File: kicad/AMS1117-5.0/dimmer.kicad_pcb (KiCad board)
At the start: 2 copper layers, 25.4 x 35.6 mm, 12 parts, among them IC1 ATTINY85-S, P1 CONN_01X02, P2 CONN_01X02, Q1 Q_NMOS_GDS, SW2 TACTILE_SW, SW4 TACTILE_SW, U1 MC78L05ACH

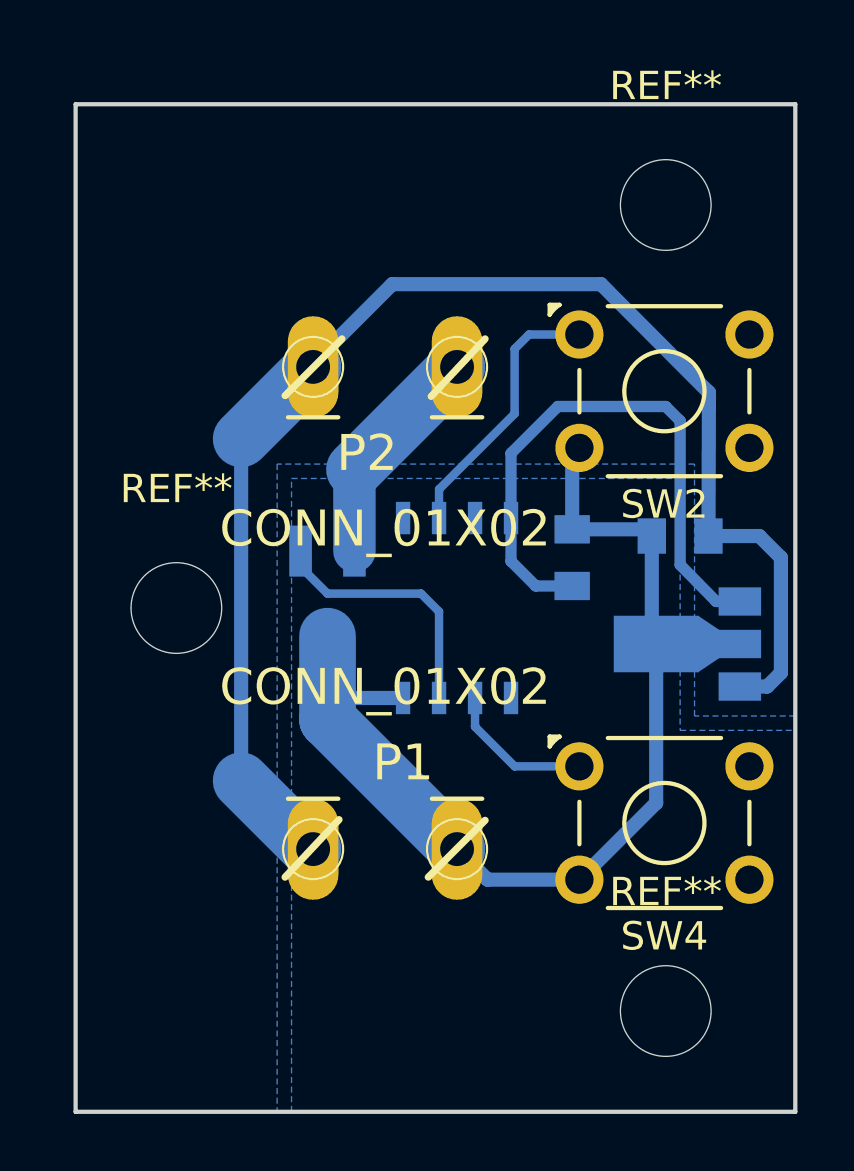
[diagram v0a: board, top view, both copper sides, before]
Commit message: AMS1117-5.0 regulator version
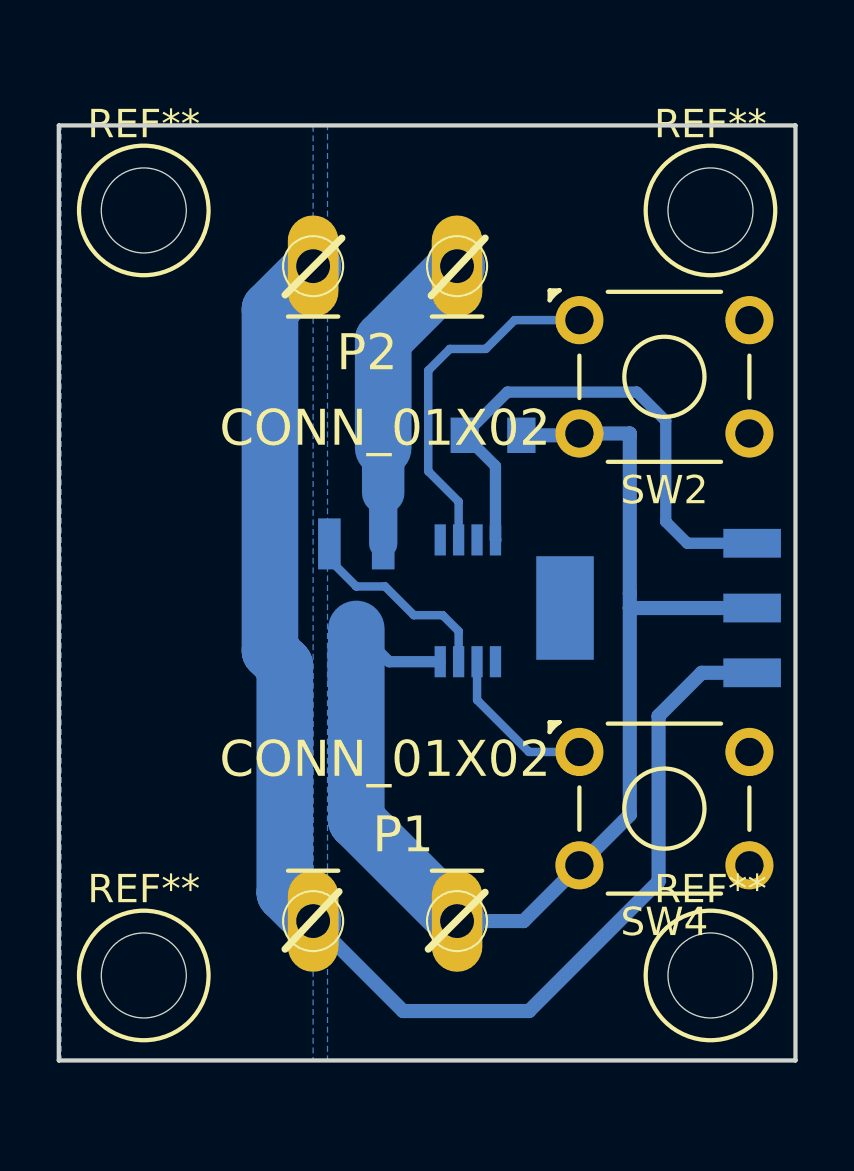
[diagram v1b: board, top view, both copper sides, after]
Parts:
- removed the REF** at (201.4, 143.3)
- removed the REF** at (201.4, 114.8)
- removed the REF** at (184.2, 129.0)
- added REF**: 1pin, Connect:1pin, F.Cu at (183.0, 115.0)
- added REF**: 1pin, Connect:1pin, F.Cu at (183.0, 142.0)
- added REF**: 1pin, Connect:1pin, F.Cu at (203.0, 142.0)
- added REF**: 1pin, Connect:1pin, F.Cu at (203.0, 115.0)
- IC1: value ATTINY85-S -> ATTINY85-P; footprint SMD_Packages:SOIC-8-N -> Housings_SSOP:TSSOP-8_3x3mm_Pitch0.65mm
- U1: footprint TO_SOT_Packages_SMD:SOT89-3_Housing -> TO_SOT_Packages_SMD:SOT-223
- moved C1 13.7 mm to (189.0, 131.1), turned to 0 degrees
- moved C2 5.14 mm to (195.3, 122.9), turned to 0 degrees
- moved P2 3.56 mm to (191.5, 116.3)
- moved P1 2.54 mm to (191.5, 140.7)
- moved U1 1.63 mm to (201.2, 129.0)
- moved Q1 1.05 mm to (190.5, 128.3)
- moved SW4 0.51 mm to (198.4, 134.1)
- moved SW2 0.51 mm to (198.4, 118.9)
- moved IC1 0.46 mm to (194.4, 128.8), turned to 90 degrees
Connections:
- IC1 pad 1: (no net) -> Net-(IC1-Pad1)
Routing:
- net GND: track 39.8 -> 46.1 mm
- net Net-(IC1-Pad6): track 9.57 -> 12.7 mm
- net /out: track 8.00 -> 10.9 mm
- net Net-(IC1-Pad3): track 9.14 -> 7.24 mm
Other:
- board size 25.4 x 35.6 mm -> 26 x 33 mm
- net class 5V: via_dia 0.6 -> 1.5; via_drill 0.4 -> 0.8

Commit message: AMS1117 correct footprint
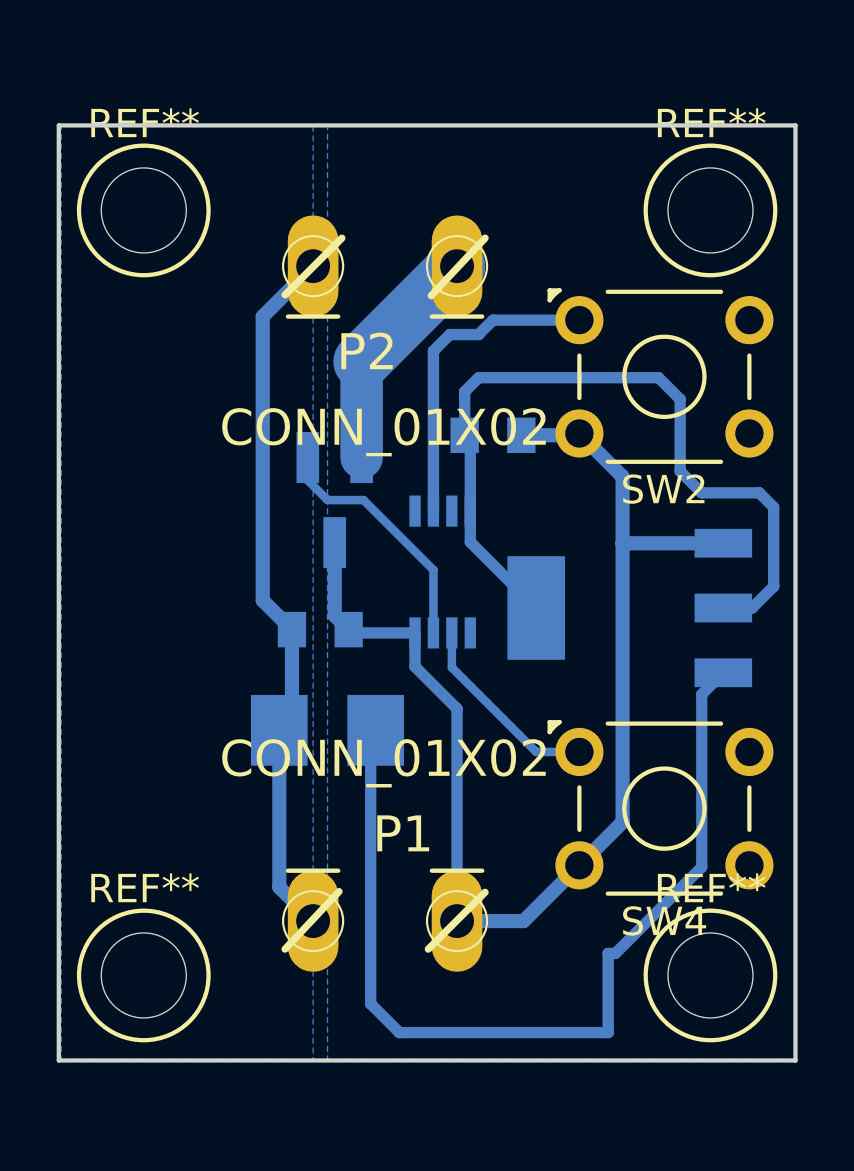
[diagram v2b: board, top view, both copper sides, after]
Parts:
- added D1: D_Small, Diodes_SMD:DO-214BA, B.Cu at (189.5, 133.3)
- IC1: value ATTINY85-P -> ATTINY85-S
- U1: value MC78L05ACH -> AMS1117-5.0
- moved Q1 3.14 mm to (189.7, 125.2)
- moved IC1 1.35 mm to (193.5, 127.8)
- moved C1 1.30 mm to (189.2, 129.8)
- moved U1 1.02 mm to (200.2, 129.0)
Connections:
- IC1 pad 1: Net-(IC1-Pad1) -> (no net)
- U1 pad 1: +5V -> GND
- U1 pad 2: GND -> +5V
- U1 pad 3: +12V -> Net-(D1-Pad1)
- U1 pad 4: (no net) -> +5V
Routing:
- net Net-(D1-Pad1): track 0.00 -> 33.1 mm
- net +12V: track 49.6 -> 25.0 mm
- net +5V: track 21.2 -> 28.1 mm
- net /out: track 10.9 -> 8.15 mm
- net Net-(IC1-Pad3): track 7.24 -> 8.82 mm
- net Net-(IC1-Pad6): track 12.7 -> 11.3 mm
- net Net-(IC1-Pad2): track 5.72 -> 6.96 mm
- net GND: track 46.1 -> 45.4 mm

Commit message: AMS117 PCB version: fixed attyny85 footprint
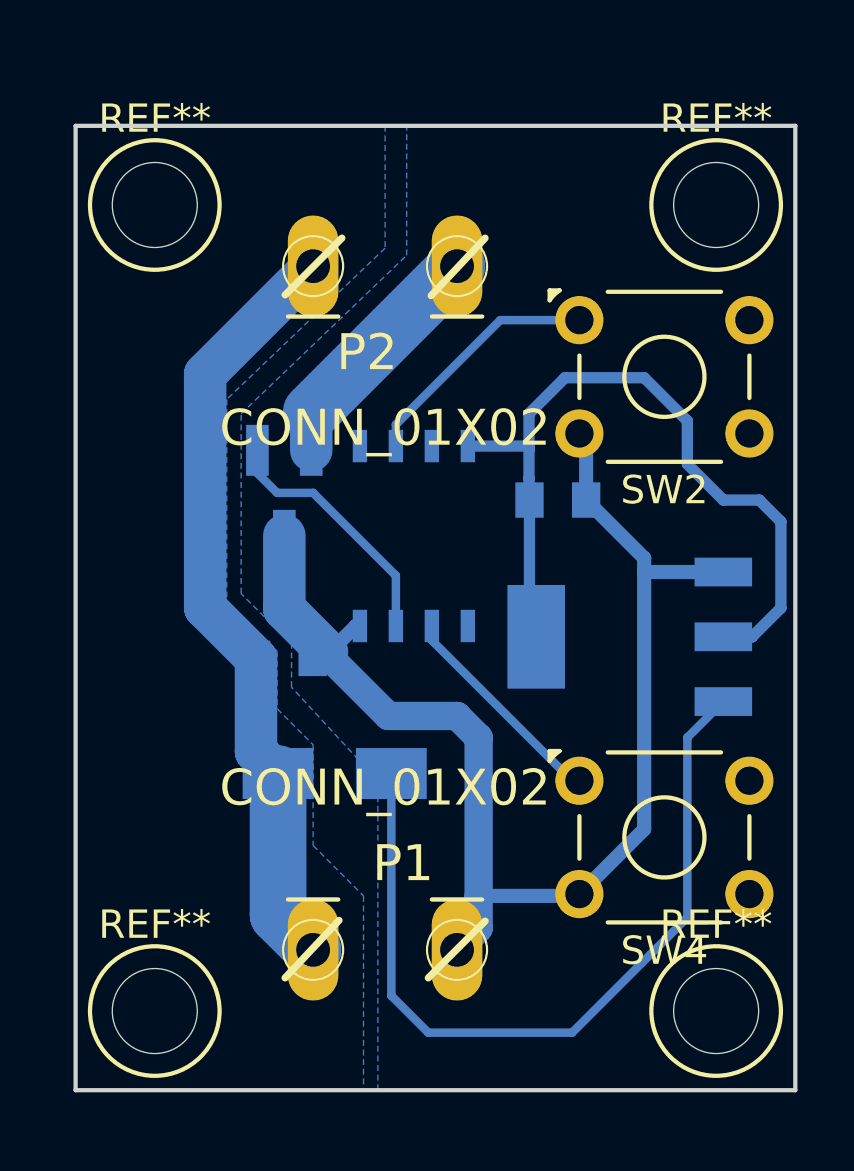
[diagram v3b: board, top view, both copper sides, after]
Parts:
- D1: footprint Diodes_SMD:DO-214BA -> Diodes_SMD:SMA_Standard
- IC1: footprint Housings_SSOP:TSSOP-8_3x3mm_Pitch0.65mm -> SMD_Packages:SOIC-8-N
- moved C2 3.23 mm to (197.6, 125.2)
- moved Q1 1.80 mm to (188.0, 125.0)
- moved IC1 1.63 mm to (192.5, 126.5), turned to 180 degrees
- moved C1 1.63 mm to (188.0, 130.8)
- moved D1 1.55 mm to (189.7, 134.9)
- moved REF** 1.31 mm to (183.4, 143.3)
- moved REF** 1.27 mm to (203.2, 143.3)
- moved P1 1.02 mm to (191.5, 141.7)
- moved SW4 1.02 mm to (198.4, 135.1)
- moved U1 1.02 mm to (200.2, 130.0)
- moved REF** 0.43 mm to (183.4, 114.8)
- moved REF** 0.28 mm to (203.2, 114.8)
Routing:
- net Net-(D1-Pad1): track 33.1 -> 29.0 mm
- net Net-(IC1-Pad6): track 11.3 -> 8.76 mm
- net +12V: track 25.0 -> 27.3 mm
- net Net-(IC1-Pad2): track 6.96 -> 8.27 mm
- net +5V: track 28.1 -> 29.1 mm
- net GND: track 45.4 -> 45.9 mm
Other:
- board size 26 x 33 mm -> 25.4 x 34 mm
